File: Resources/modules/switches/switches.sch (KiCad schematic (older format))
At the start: 44 parts, among them J1 switchesOut, J10 Conn_01x01_Female, J11 Conn_01x01_Female, J12 Conn_01x01_Female, J2 Conn_01x01_Female, J3 Conn_01x01_Female, J4 Conn_01x01_Female, J5 Conn_01x01_Female, J6 Conn_01x01_Female, J7 Conn_01x01_Female, J8 Conn_01x01_Female, J9 Conn_01x01_Female, Q1 2N7002, Q2 2N7002, Q3 2N7002, Q4 2N7002, Q5 2N7002, Q6 2N7002

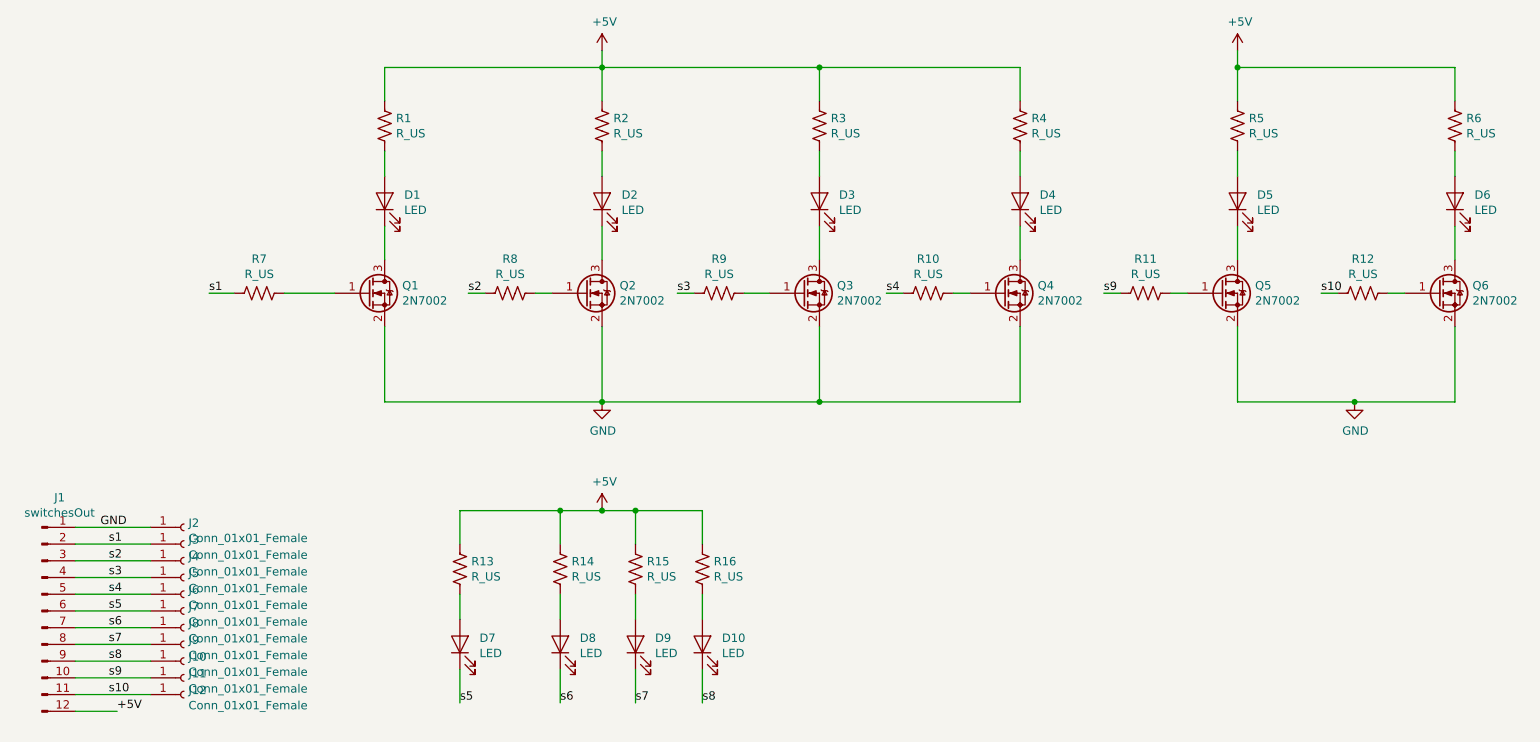
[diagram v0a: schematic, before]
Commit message: altered switches-board design; shifted resistor
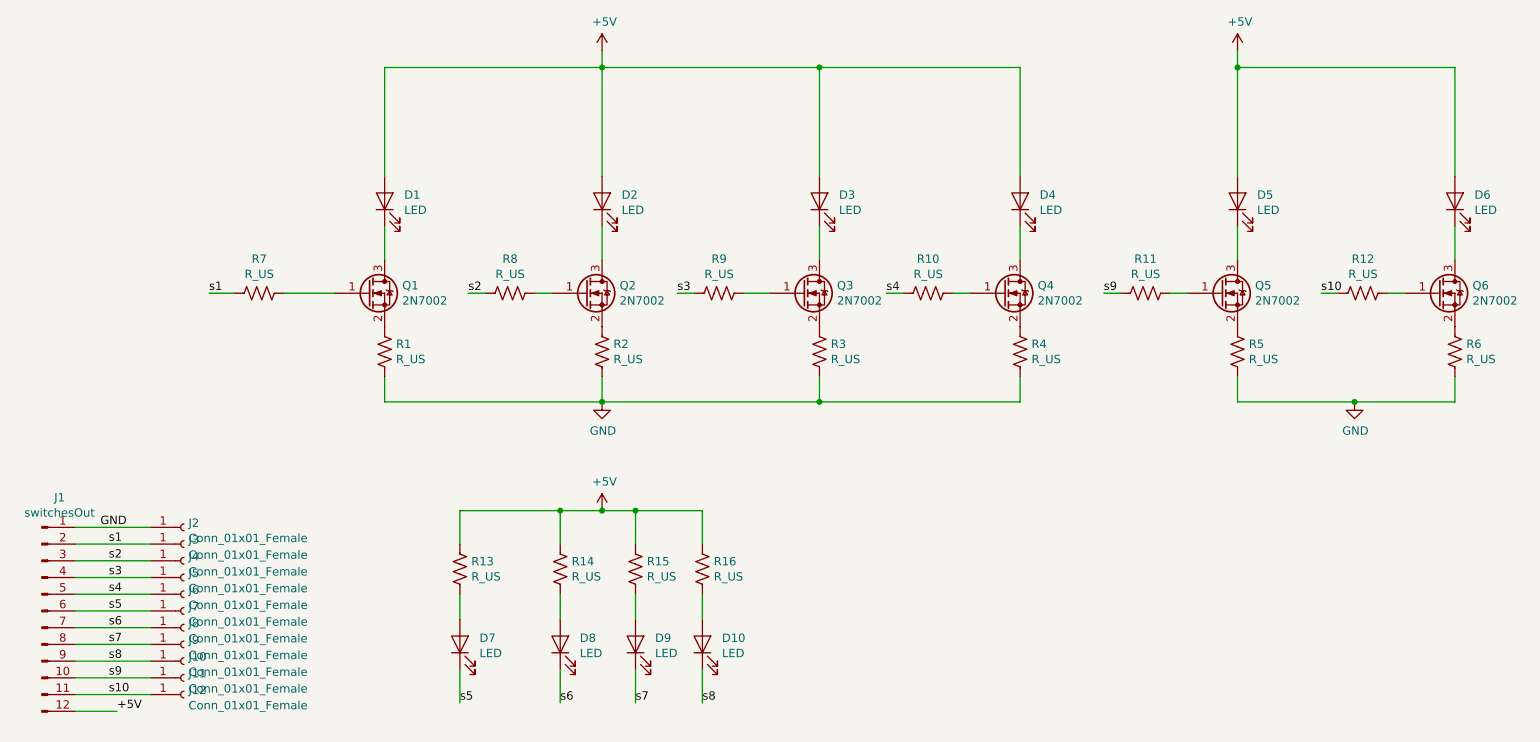
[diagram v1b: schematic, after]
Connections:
- net +5V: now also D1.2 (A), D2.2 (A), D3.2 (A), D4.2 (A), D5.2 (A), D6.2 (A); no longer R1.1, R2.1, R3.1, R4.1, R5.1, R6.1
- net GND: now also R1.2, R2.2, R3.2, R4.2, R5.2, R6.2; no longer Q1.2 (S), Q2.2 (S), Q3.2 (S), Q4.2 (S), Q5.2 (S), Q6.2 (S)
- new net: Q1.2 (S), R1.1
- new net: Q2.2 (S), R2.1
- new net: Q3.2 (S), R3.1
- new net: Q4.2 (S), R4.1
- new net: Q5.2 (S), R5.1
- new net: Q6.2 (S), R6.1
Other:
- moved on the sheet: R1, R2, R3, R4, R5, R6
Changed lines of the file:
@@
 L Device:R_US R1
 U 1 1 5C388E52
-P 4000 1150
-F 0 "R1" H 4068 1196 50  0000 L CNN
-F 1 "R_US" H 4068 1105 50  0000 L CNN
-F 2 "Resistors_SMD:R_0805_HandSoldering" V 4040 1140 50  0001 C CNN
-F 3 "~" H 4000 1150 50  0001 C CNN
-	1    4000 1150
+P 4000 2500
+F 0 "R1" H 4068 2546 50  0000 L CNN
+F 1 "R_US" H 4068 2455 50  0000 L CNN
+F 2 "Resistors_SMD:R_0805_HandSoldering" V 4040 2490 50  0001 C CNN
+F 3 "~" H 4000 2500 50  0001 C CNN
+	1    4000 2500
 	1    0    0    -1
 $EndComp
@@
 L Device:R_US R2
 U 1 1 5C38A292
-P 5300 1150
-F 0 "R2" H 5368 1196 50  0000 L CNN
-F 1 "R_US" H 5368 1105 50  0000 L CNN
-F 2 "Resistors_SMD:R_0805_HandSoldering" V 5340 1140 50  0001 C CNN
-F 3 "~" H 5300 1150 50  0001 C CNN
-	1    5300 1150
+P 5300 2500
+F 0 "R2" H 5368 2546 50  0000 L CNN
+F 1 "R_US" H 5368 2455 50  0000 L CNN
+F 2 "Resistors_SMD:R_0805_HandSoldering" V 5340 2490 50  0001 C CNN
+F 3 "~" H 5300 2500 50  0001 C CNN
+	1    5300 2500
 	1    0    0    -1
 $EndComp
@@
 L Device:R_US R3
 U 1 1 5C38A2F8
-P 6600 1150
-F 0 "R3" H 6668 1196 50  0000 L CNN
-F 1 "R_US" H 6668 1105 50  0000 L CNN
-F 2 "Resistors_SMD:R_0805_HandSoldering" V 6640 1140 50  0001 C CNN
-F 3 "~" H 6600 1150 50  0001 C CNN
-	1    6600 1150
+P 6600 2500
+F 0 "R3" H 6668 2546 50  0000 L CNN
+F 1 "R_US" H 6668 2455 50  0000 L CNN
+F 2 "Resistors_SMD:R_0805_HandSoldering" V 6640 2490 50  0001 C CNN
+F 3 "~" H 6600 2500 50  0001 C CNN
+	1    6600 2500
 	1    0    0    -1
 $EndComp
@@
 $EndComp
 Wire Wire Line
-	4000 1300 4000 1450
-Wire Wire Line
 	4000 1750 4000 1950
 Wire Wire Line
@@
 Wire Wire Line
 	6600 1750 6600 1950
-Wire Wire Line
-	5300 1300 5300 1450
-Wire Wire Line
-	6600 1300 6600 1450
-Wire Wire Line
-	4000 1000 4000 800
-Wire Wire Line
-	6600 800  6600 1000
-Wire Wire Line
-	5300 1000 5300 800
 Wire Wire Line
 	4000 800  5300 800
@@
 	5300 700  5300 800
 Wire Wire Line
-	4000 2350 4000 2800
-Wire Wire Line
 	4000 2800 5300 2800
-Wire Wire Line
-	6600 2800 6600 2350
-Wire Wire Line
-	5300 2350 5300 2800
 Connection ~ 5300 2800
-Wire Wire Line
-	5300 2800 6600 2800
 $Comp
 L power:GND #PWR0102
@@
 L Device:R_US R4
 U 1 1 5C390638
-P 7800 1150
-F 0 "R4" H 7868 1196 50  0000 L CNN
-F 1 "R_US" H 7868 1105 50  0000 L CNN
-F 2 "Resistors_SMD:R_0805_HandSoldering" V 7840 1140 50  0001 C CNN
-F 3 "~" H 7800 1150 50  0001 C CNN
-	1    7800 1150
+P 7800 2500
+F 0 "R4" H 7868 2546 50  0000 L CNN
+F 1 "R_US" H 7868 2455 50  0000 L CNN
+F 2 "Resistors_SMD:R_0805_HandSoldering" V 7840 2490 50  0001 C CNN
+F 3 "~" H 7800 2500 50  0001 C CNN
+	1    7800 2500
 	1    0    0    -1
 $EndComp
@@
 L Device:R_US R5
 U 1 1 5C39063F
-P 9100 1150
-F 0 "R5" H 9168 1196 50  0000 L CNN
-F 1 "R_US" H 9168 1105 50  0000 L CNN
-F 2 "Resistors_SMD:R_0805_HandSoldering" V 9140 1140 50  0001 C CNN
-F 3 "~" H 9100 1150 50  0001 C CNN
-	1    9100 1150
+P 9100 2500
+F 0 "R5" H 9168 2546 50  0000 L CNN
+F 1 "R_US" H 9168 2455 50  0000 L CNN
+F 2 "Resistors_SMD:R_0805_HandSoldering" V 9140 2490 50  0001 C CNN
+F 3 "~" H 9100 2500 50  0001 C CNN
+	1    9100 2500
 	1    0    0    -1
 $EndComp
@@
 L Device:R_US R6
 U 1 1 5C390646
-P 10400 1150
-F 0 "R6" H 10468 1196 50  0000 L CNN
-F 1 "R_US" H 10468 1105 50  0000 L CNN
-F 2 "Resistors_SMD:R_0805_HandSoldering" V 10440 1140 50  0001 C CNN
-F 3 "~" H 10400 1150 50  0001 C CNN
-	1    10400 1150
+P 10400 2500
+F 0 "R6" H 10468 2546 50  0000 L CNN
+F 1 "R_US" H 10468 2455 50  0000 L CNN
+F 2 "Resistors_SMD:R_0805_HandSoldering" V 10440 2490 50  0001 C CNN
+F 3 "~" H 10400 2500 50  0001 C CNN
+	1    10400 2500
 	1    0    0    -1
 $EndComp
@@
 $EndComp
 Wire Wire Line
-	7800 1300 7800 1450
-Wire Wire Line
 	7800 1750 7800 1950
 Wire Wire Line
@@
 Wire Wire Line
 	10400 1750 10400 1950
-Wire Wire Line
-	9100 1300 9100 1450
-Wire Wire Line
-	10400 1300 10400 1450
-Wire Wire Line
-	7800 1000 7800 800
-Wire Wire Line
-	10400 800  10400 1000
-Wire Wire Line
-	9100 1000 9100 800
 Connection ~ 9100 800
 Wire Wire Line
@@
 	9100 700  9100 800
 Wire Wire Line
-	7800 2350 7800 2800
-Wire Wire Line
-	10400 2800 10400 2350
-Wire Wire Line
-	9100 2350 9100 2800
-Wire Wire Line
 	9100 2800 9800 2800
 $Comp
@@
 Wire Wire Line
 	6600 800  7800 800
-Wire Wire Line
-	7800 2800 6600 2800
-Connection ~ 6600 2800
 Connection ~ 9800 2800
-Wire Wire Line
-	9800 2800 10400 2800
 $Comp
 L Connector:Conn_01x12_Male J1
@@
 Wire Wire Line
 	5300 3450 5500 3450
+Wire Wire Line
+	5300 2800 6600 2800
+Wire Wire Line
+	4000 800  4000 1450
+Wire Wire Line
+	4000 2650 4000 2800
+Wire Wire Line
+	5300 2800 5300 2650
+Wire Wire Line
+	5300 800  5300 1450
+Wire Wire Line
+	6600 800  6600 1450
+Wire Wire Line
+	6600 2650 6600 2800
+Connection ~ 6600 2800
+Wire Wire Line
+	6600 2800 7800 2800
+Wire Wire Line
+	7800 800  7800 1450
+Wire Wire Line
+	7800 2650 7800 2800
+Wire Wire Line
+	9100 800  9100 1450
+Wire Wire Line
+	10400 800  10400 1450
+Wire Wire Line
+	10400 2650 10400 2800
+Wire Wire Line
+	9800 2800 10400 2800
+Wire Wire Line
+	9100 2650 9100 2800
 $EndSCHEMATC

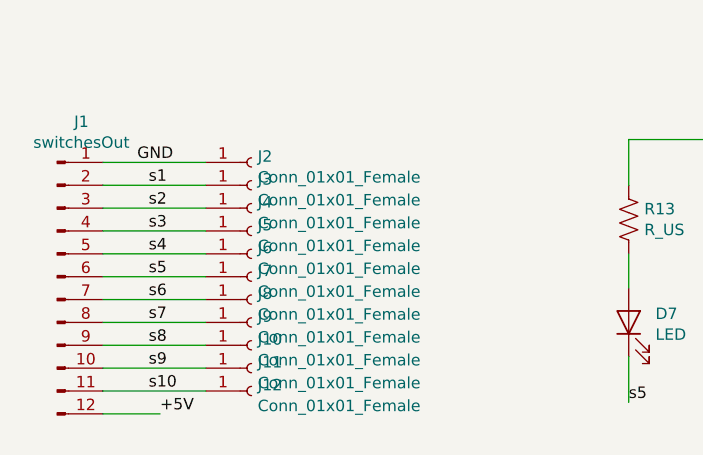
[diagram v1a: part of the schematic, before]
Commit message: label correction&additions in traffic&switches modules. Updated gerbers - both V1 and modules
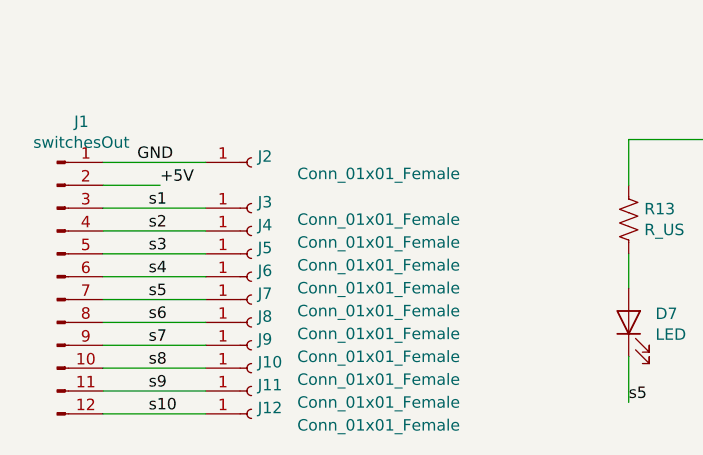
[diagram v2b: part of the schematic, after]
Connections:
- net +5V: now also J1.2 (Pin_2); no longer J1.12 (Pin_12)
- net s1: now also J1.3 (Pin_3); no longer J1.2 (Pin_2)
- net s10: now also J1.12 (Pin_12); no longer J1.11 (Pin_11)
- net s2: now also J1.4 (Pin_4); no longer J1.3 (Pin_3)
- net s3: now also J1.5 (Pin_5); no longer J1.4 (Pin_4)
- net s4: now also J1.6 (Pin_6); no longer J1.5 (Pin_5)
- net s5: now also J1.7 (Pin_7); no longer J1.6 (Pin_6)
- net s6: now also J1.8 (Pin_8); no longer J1.7 (Pin_7)
- net s7: now also J1.9 (Pin_9); no longer J1.8 (Pin_8)
- net s8: now also J1.10 (Pin_10); no longer J1.9 (Pin_9)
- net s9: now also J1.11 (Pin_11); no longer J1.10 (Pin_10)
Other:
- moved on the sheet: J10, J11, J12, J3, J4, J5, J6, J7, J8, J9
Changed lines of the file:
@@
 	2150 3550 2600 3550
 Wire Wire Line
-	2150 3650 2600 3650
-Wire Wire Line
 	2150 3750 2600 3750
 Wire Wire Line
@@
 Wire Wire Line
 	2150 4550 2600 4550
+Wire Wire Line
+	2150 4650 2600 4650
 Text Label 2300 3550 0    50   ~ 0
 GND
-Text Label 2350 3650 0    50   ~ 0
+Text Label 2350 3750 0    50   ~ 0
 s1
-Text Label 2350 3750 0    50   ~ 0
+Text Label 2350 3850 0    50   ~ 0
 s2
-Text Label 2350 3850 0    50   ~ 0
+Text Label 2350 3950 0    50   ~ 0
 s3
-Text Label 2350 3950 0    50   ~ 0
+Text Label 2350 4050 0    50   ~ 0
 s4
-Text Label 2350 4050 0    50   ~ 0
+Text Label 2350 4150 0    50   ~ 0
 s5
-Text Label 2350 4150 0    50   ~ 0
+Text Label 2350 4250 0    50   ~ 0
 s6
-Text Label 2350 4250 0    50   ~ 0
+Text Label 2350 4350 0    50   ~ 0
 s7
-Text Label 2350 4350 0    50   ~ 0
+Text Label 2350 4450 0    50   ~ 0
 s8
-Text Label 2350 4450 0    50   ~ 0
+Text Label 2350 4550 0    50   ~ 0
 s9
-Text Label 2350 4550 0    50   ~ 0
+Text Label 2350 4650 0    50   ~ 0
 s10
 $Comp
@@
 P 2800 3550
 F 0 "J2" H 2827 3576 50  0000 L CNN
-F 1 "Conn_01x01_Female" H 2827 3485 50  0000 L CNN
+F 1 "Conn_01x01_Female" H 3000 3500 50  0000 L CNN
 F 2 "Wire_Pads:SolderWirePad_single_SMD_5x10mm" H 2800 3550 50  0001 C CNN
 F 3 "~" H 2800 3550 50  0001 C CNN
@@
 L Connector:Conn_01x01_Female J3
 U 1 1 5C3723D4
-P 2800 3650
-F 0 "J3" H 2827 3676 50  0000 L CNN
-F 1 "Conn_01x01_Female" H 2827 3585 50  0000 L CNN
-F 2 "Wire_Pads:SolderWirePad_single_SMD_5x10mm" H 2800 3650 50  0001 C CNN
-F 3 "~" H 2800 3650 50  0001 C CNN
-	1    2800 3650
-	1    0    0    -1
-$EndComp
-$Comp
-L Connector:Conn_01x01_Female J4
-U 1 1 5C3723EA
 P 2800 3750
-F 0 "J4" H 2827 3776 50  0000 L CNN
-F 1 "Conn_01x01_Female" H 2827 3685 50  0000 L CNN
+F 0 "J3" H 2827 3776 50  0000 L CNN
+F 1 "Conn_01x01_Female" H 3000 3700 50  0000 L CNN
 F 2 "Wire_Pads:SolderWirePad_single_SMD_5x10mm" H 2800 3750 50  0001 C CNN
 F 3 "~" H 2800 3750 50  0001 C CNN
@@
 $EndComp
 $Comp
-L Connector:Conn_01x01_Female J5
-U 1 1 5C372402
+L Connector:Conn_01x01_Female J4
+U 1 1 5C3723EA
 P 2800 3850
-F 0 "J5" H 2827 3876 50  0000 L CNN
-F 1 "Conn_01x01_Female" H 2827 3785 50  0000 L CNN
+F 0 "J4" H 2827 3876 50  0000 L CNN
+F 1 "Conn_01x01_Female" H 3000 3800 50  0000 L CNN
 F 2 "Wire_Pads:SolderWirePad_single_SMD_5x10mm" H 2800 3850 50  0001 C CNN
 F 3 "~" H 2800 3850 50  0001 C CNN
@@
 $EndComp
 $Comp
-L Connector:Conn_01x01_Female J6
-U 1 1 5C37241C
+L Connector:Conn_01x01_Female J5
+U 1 1 5C372402
 P 2800 3950
-F 0 "J6" H 2827 3976 50  0000 L CNN
-F 1 "Conn_01x01_Female" H 2827 3885 50  0000 L CNN
+F 0 "J5" H 2827 3976 50  0000 L CNN
+F 1 "Conn_01x01_Female" H 3000 3900 50  0000 L CNN
 F 2 "Wire_Pads:SolderWirePad_single_SMD_5x10mm" H 2800 3950 50  0001 C CNN
 F 3 "~" H 2800 3950 50  0001 C CNN
@@
 $EndComp
 $Comp
-L Connector:Conn_01x01_Female J7
-U 1 1 5C372438
+L Connector:Conn_01x01_Female J6
+U 1 1 5C37241C
 P 2800 4050
-F 0 "J7" H 2827 4076 50  0000 L CNN
-F 1 "Conn_01x01_Female" H 2827 3985 50  0000 L CNN
+F 0 "J6" H 2827 4076 50  0000 L CNN
+F 1 "Conn_01x01_Female" H 3000 4000 50  0000 L CNN
 F 2 "Wire_Pads:SolderWirePad_single_SMD_5x10mm" H 2800 4050 50  0001 C CNN
 F 3 "~" H 2800 4050 50  0001 C CNN
@@
 $EndComp
 $Comp
-L Connector:Conn_01x01_Female J8
-U 1 1 5C372456
+L Connector:Conn_01x01_Female J7
+U 1 1 5C372438
 P 2800 4150
-F 0 "J8" H 2827 4176 50  0000 L CNN
-F 1 "Conn_01x01_Female" H 2827 4085 50  0000 L CNN
+F 0 "J7" H 2827 4176 50  0000 L CNN
+F 1 "Conn_01x01_Female" H 3000 4100 50  0000 L CNN
 F 2 "Wire_Pads:SolderWirePad_single_SMD_5x10mm" H 2800 4150 50  0001 C CNN
 F 3 "~" H 2800 4150 50  0001 C CNN
@@
 $EndComp
 $Comp
-L Connector:Conn_01x01_Female J9
-U 1 1 5C372476
+L Connector:Conn_01x01_Female J8
+U 1 1 5C372456
 P 2800 4250
-F 0 "J9" H 2827 4276 50  0000 L CNN
-F 1 "Conn_01x01_Female" H 2827 4185 50  0000 L CNN
+F 0 "J8" H 2827 4276 50  0000 L CNN
+F 1 "Conn_01x01_Female" H 3000 4200 50  0000 L CNN
 F 2 "Wire_Pads:SolderWirePad_single_SMD_5x10mm" H 2800 4250 50  0001 C CNN
 F 3 "~" H 2800 4250 50  0001 C CNN
@@
 $EndComp
 $Comp
-L Connector:Conn_01x01_Female J10
-U 1 1 5C372498
+L Connector:Conn_01x01_Female J9
+U 1 1 5C372476
 P 2800 4350
-F 0 "J10" H 2827 4376 50  0000 L CNN
-F 1 "Conn_01x01_Female" H 2827 4285 50  0000 L CNN
+F 0 "J9" H 2827 4376 50  0000 L CNN
+F 1 "Conn_01x01_Female" H 3000 4300 50  0000 L CNN
 F 2 "Wire_Pads:SolderWirePad_single_SMD_5x10mm" H 2800 4350 50  0001 C CNN
 F 3 "~" H 2800 4350 50  0001 C CNN
@@
 $EndComp
 $Comp
-L Connector:Conn_01x01_Female J11
-U 1 1 5C3724BC
+L Connector:Conn_01x01_Female J10
+U 1 1 5C372498
 P 2800 4450
-F 0 "J11" H 2827 4476 50  0000 L CNN
-F 1 "Conn_01x01_Female" H 2827 4385 50  0000 L CNN
+F 0 "J10" H 2827 4476 50  0000 L CNN
+F 1 "Conn_01x01_Female" H 3000 4400 50  0000 L CNN
 F 2 "Wire_Pads:SolderWirePad_single_SMD_5x10mm" H 2800 4450 50  0001 C CNN
 F 3 "~" H 2800 4450 50  0001 C CNN
@@
 $EndComp
 $Comp
-L Connector:Conn_01x01_Female J12
-U 1 1 5C3724E2
+L Connector:Conn_01x01_Female J11
+U 1 1 5C3724BC
 P 2800 4550
-F 0 "J12" H 2827 4576 50  0000 L CNN
-F 1 "Conn_01x01_Female" H 2827 4485 50  0000 L CNN
+F 0 "J11" H 2827 4576 50  0000 L CNN
+F 1 "Conn_01x01_Female" H 3000 4500 50  0000 L CNN
 F 2 "Wire_Pads:SolderWirePad_single_SMD_5x10mm" H 2800 4550 50  0001 C CNN
 F 3 "~" H 2800 4550 50  0001 C CNN
 	1    2800 4550
+	1    0    0    -1
+$EndComp
+$Comp
+L Connector:Conn_01x01_Female J12
+U 1 1 5C3724E2
+P 2800 4650
+F 0 "J12" H 2827 4676 50  0000 L CNN
+F 1 "Conn_01x01_Female" H 3000 4600 50  0000 L CNN
+F 2 "Wire_Pads:SolderWirePad_single_SMD_5x10mm" H 2800 4650 50  0001 C CNN
+F 3 "~" H 2800 4650 50  0001 C CNN
+	1    2800 4650
 	1    0    0    -1
 $EndComp
@@
 $EndComp
 Wire Wire Line
-	2400 4650 2150 4650
+	2400 3650 2150 3650
 $Comp
 L Device:R_US R7
@@
 Text Label 9600 2150 0    50   ~ 0
 s10
-Text Label 2400 4650 0    50   ~ 0
+Text Label 2400 3650 0    50   ~ 0
 +5V
 $Comp
